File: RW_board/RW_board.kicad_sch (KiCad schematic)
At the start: 0 parts

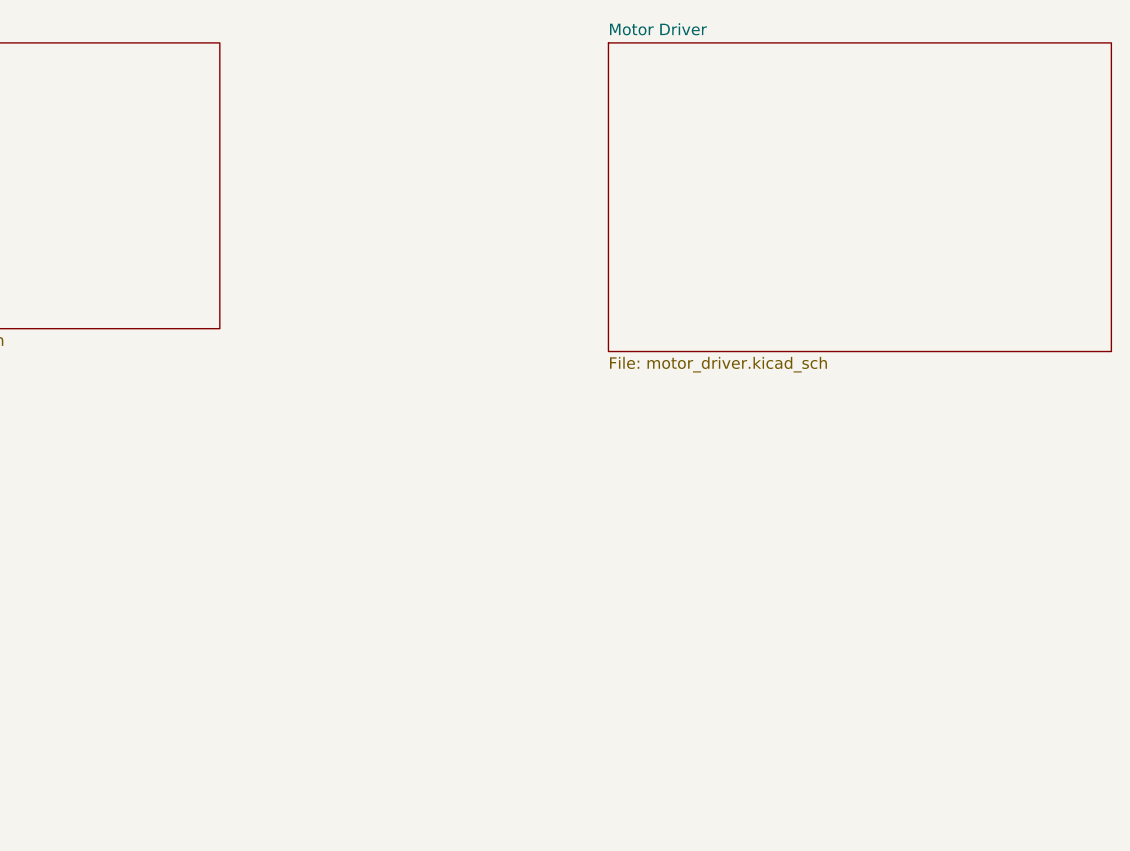
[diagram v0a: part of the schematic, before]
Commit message: Started working on motor driver schematic, added libraries, added motor cad
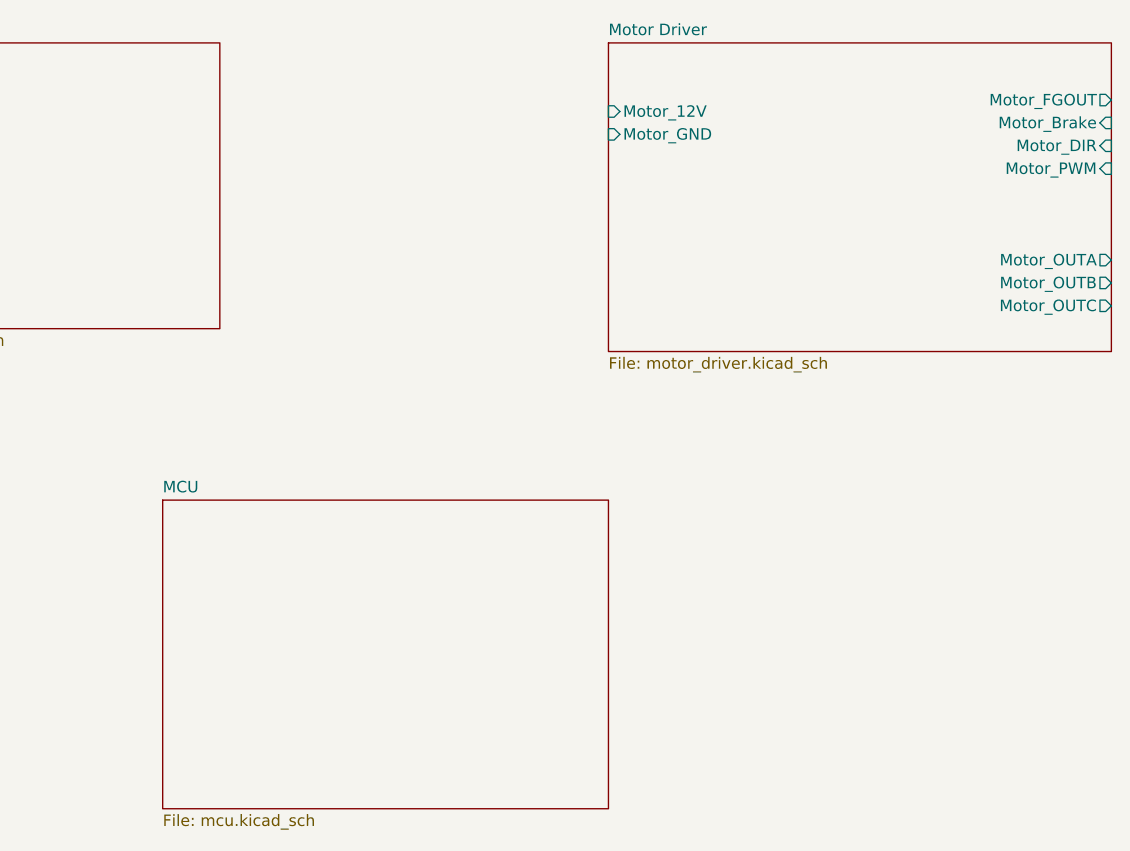
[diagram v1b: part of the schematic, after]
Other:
- added sheet MCU (mcu.kicad_sch)
- sheet Motor Driver ports: added Motor_12V, Motor_Brake, Motor_DIR, Motor_FGOUT, Motor_GND, Motor_OUTA, Motor_OUTB, Motor_OUTC, Motor_PWM; removed none
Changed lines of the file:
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@@
+			)
+		)
+		(pin "Motor_12V" input
+			(at 146.05 58.42 180)
+			(effects
+				(font
+					(size 1.27 1.27)
+				)
+				(justify left)
+			)
+		)
+		(pin "Motor_GND" input
+			(at 146.05 60.96 180)
+			(effects
+				(font
+					(size 1.27 1.27)
+				)
+				(justify left)
+			)
+		)
+		(pin "Motor_FGOUT" output
+			(at 201.93 57.15 0)
+			(effects
+				(font
+					(size 1.27 1.27)
+				)
+				(justify right)
+			)
+		)
+		(pin "Motor_Brake" input
+			(at 201.93 59.69 0)
+			(effects
+				(font
+					(size 1.27 1.27)
+				)
+				(justify right)
+			)
+		)
+		(pin "Motor_DIR" input
+			(at 201.93 62.23 0)
+			(effects
+				(font
+					(size 1.27 1.27)
+				)
+				(justify right)
+			)
+		)
+		(pin "Motor_PWM" input
+			(at 201.93 64.77 0)
+			(effects
+				(font
+					(size 1.27 1.27)
+				)
+				(justify right)
+			)
+		)
+		(pin "Motor_OUTB" output
+			(at 201.93 77.47 0)
+			(effects
+				(font
+					(size 1.27 1.27)
+				)
+				(justify right)
+			)
+		)
+		(pin "Motor_OUTC" output
+			(at 201.93 80.01 0)
+			(effects
+				(font
+					(size 1.27 1.27)
+				)
+				(justify right)
+			)
+		)
+		(pin "Motor_OUTA" output
+			(at 201.93 74.93 0)
+			(effects
+				(font
+					(size 1.27 1.27)
+				)
+				(justify right)
 			)
 		)
@@
 				)
 			)
+		)
+	)
+	(sheet
+		(at 96.52 101.6)
+		(size 49.53 34.29)
+		(fields_autoplaced yes)
+		(stroke
+			(width 0.1524)
+			(type solid)
+		)
+		(fill
+			(color 0 0 0 0.0000)
+		)
+		(property "Sheetname" "MCU"
+			(at 96.52 100.8884 0)
+			(effects
+				(font
+					(size 1.27 1.27)
+				)
+				(justify left bottom)
+			)
+		)
+		(property "Sheetfile" "mcu.kicad_sch"
+			(at 96.52 136.4746 0)
+			(effects
+				(font
+					(size 1.27 1.27)
+				)
+				(justify left top)
+			)
+		)
+		(instances
+			(project "RW_board"
+				(path "/ff273890-9ca6-499d-9c73-a93557b69e48"
+					(page "4")
+				)
+			)

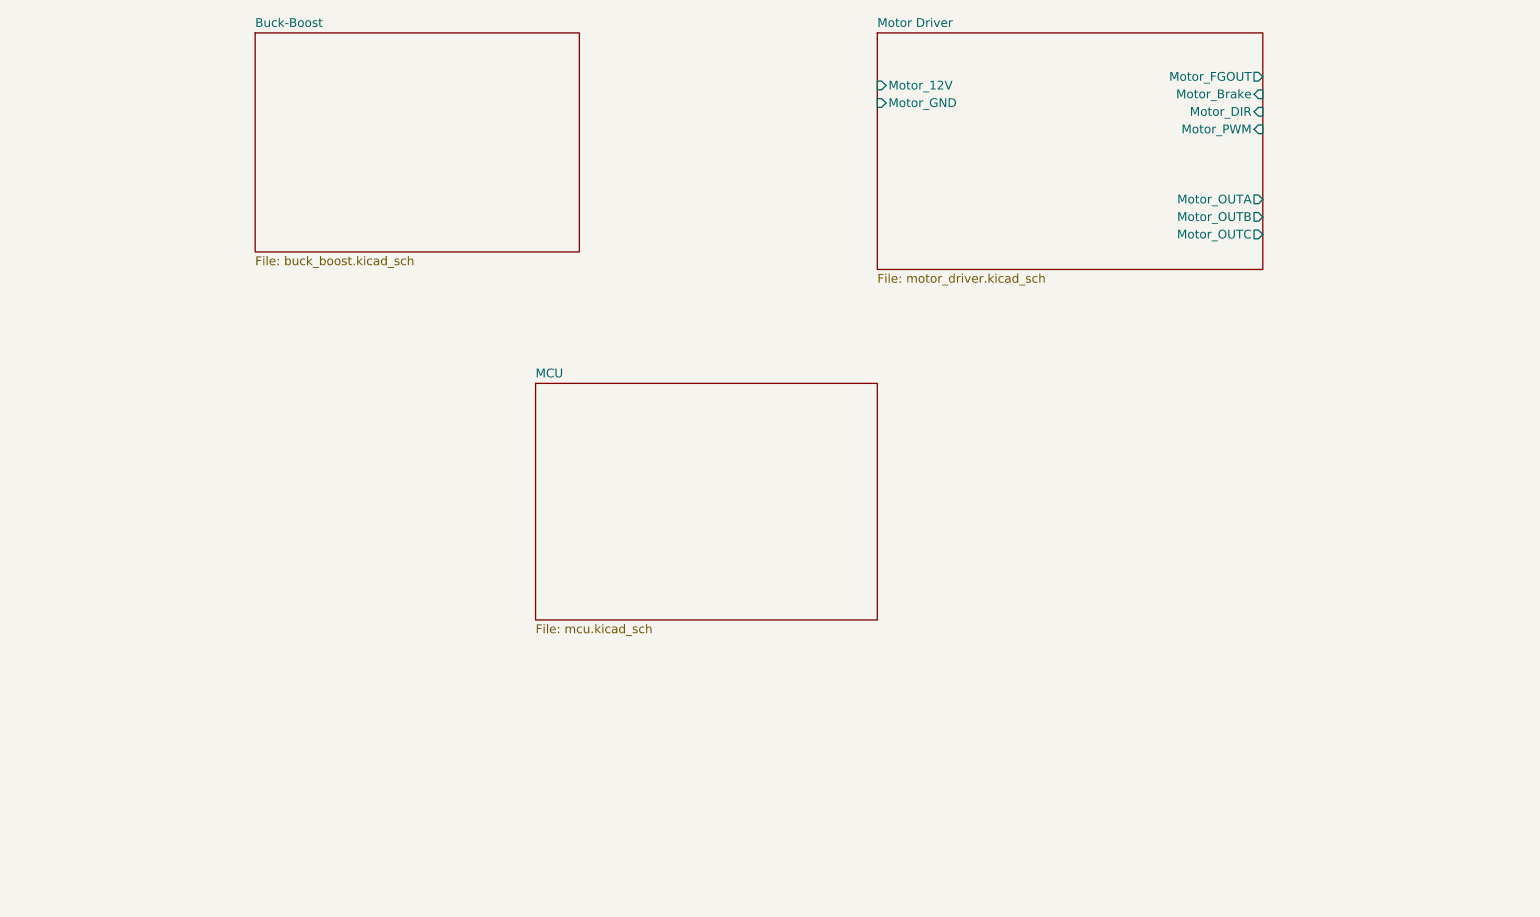
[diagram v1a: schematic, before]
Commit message: Added motor symbol/footprint, worked more on schematic
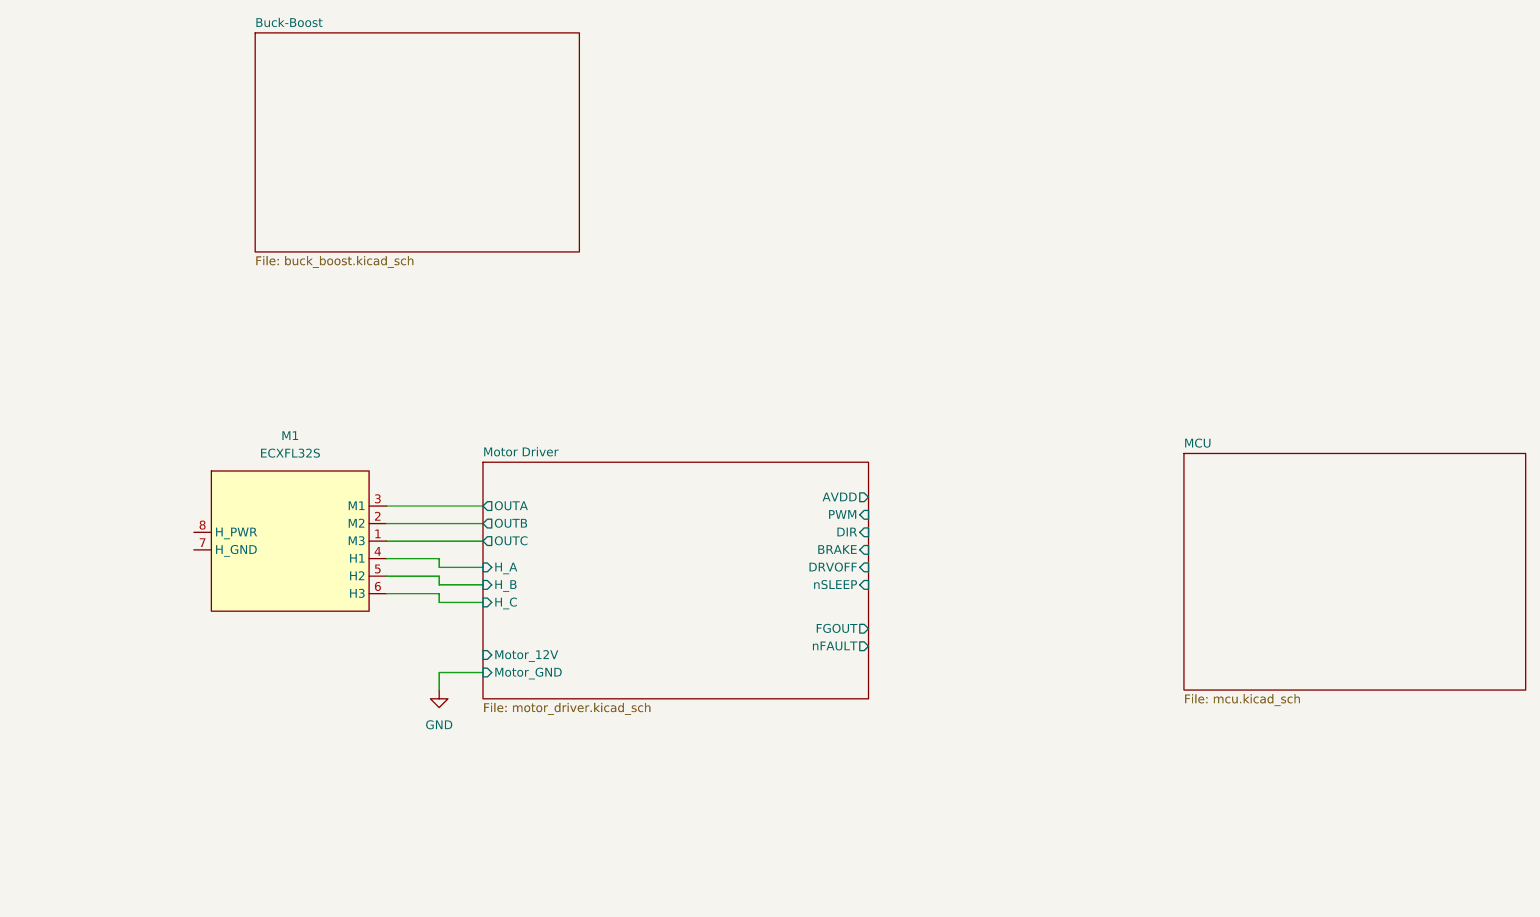
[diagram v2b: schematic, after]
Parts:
- added M1: ECXFL32S, ECXFL32S:ECXFL32S, symbol ECXFL32S:ECXFL32S
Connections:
- new net Motor Driver/H_A: M1.4 (H1)
- new net Motor Driver/H_B: M1.5 (H2)
- new net Motor Driver/H_C: M1.6 (H3)
- new net Motor Driver/OUTA: M1.3 (M1)
- new net Motor Driver/OUTB: M1.2 (M2)
- new net Motor Driver/OUTC: M1.1 (M3)
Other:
- sheet Motor Driver ports: added AVDD, BRAKE, DIR, DRVOFF, FGOUT, H_A, H_B, H_C, OUTA, OUTB, OUTC, PWM, nFAULT, nSLEEP; removed Motor_Brake, Motor_DIR, Motor_FGOUT, Motor_OUTA, Motor_OUTB, Motor_OUTC, Motor_PWM

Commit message: Completed MCU schematic, connected with driver schematic
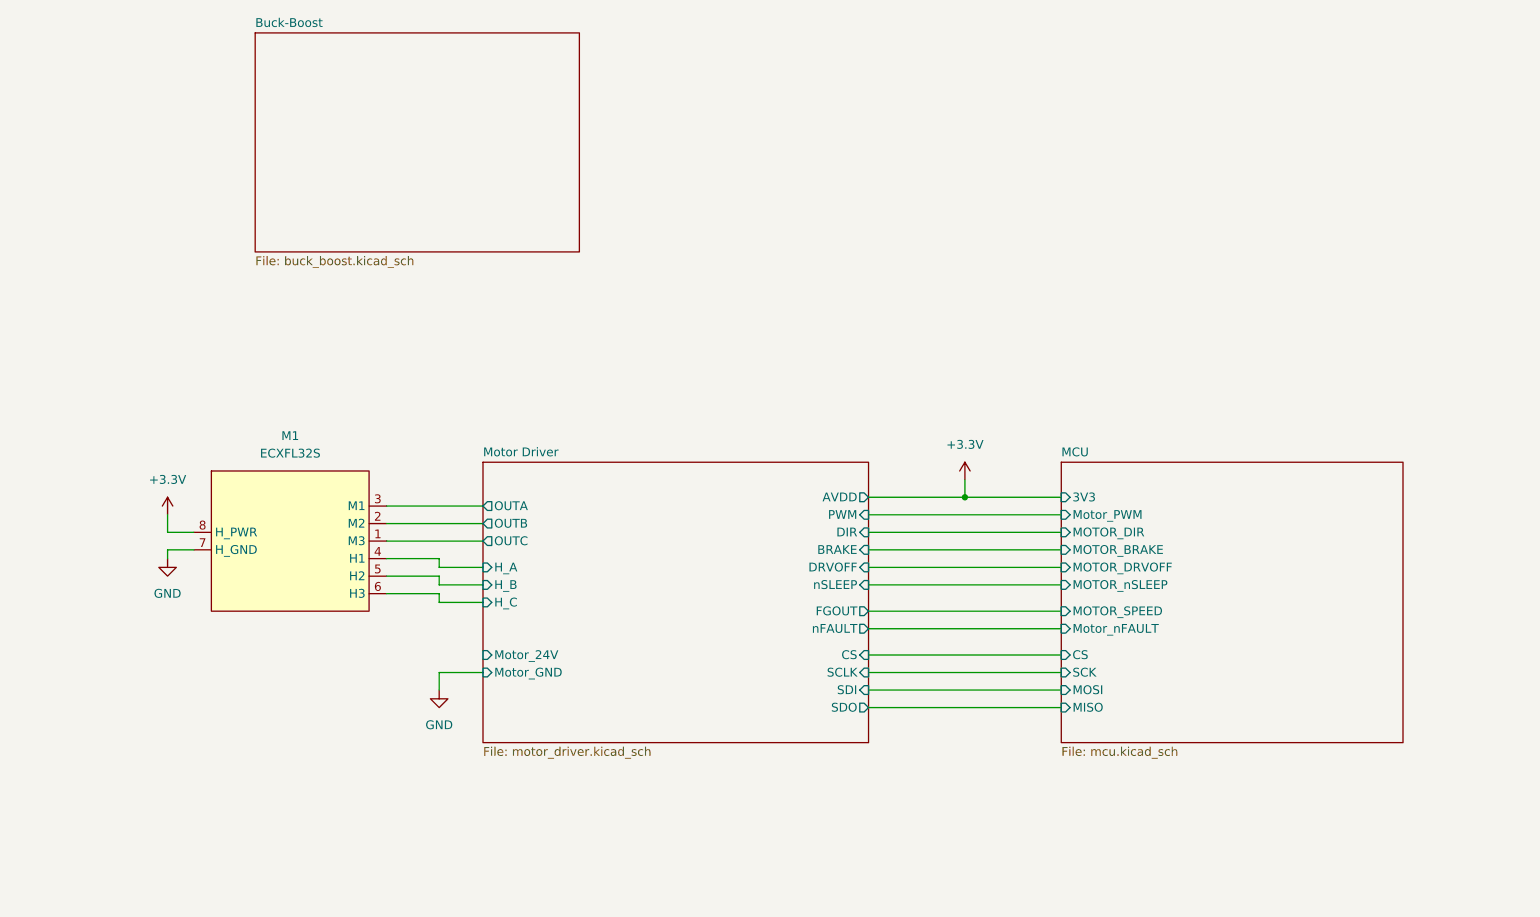
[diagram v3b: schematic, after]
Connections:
- net GND: now also M1.7 (H_GND)
- net +3.3V: now reaches M1.8 (H_PWR)
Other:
- sheet MCU ports: added 3V3, CS, MISO, MOSI, MOTOR_BRAKE, MOTOR_DIR, MOTOR_DRVOFF, MOTOR_SPEED, MOTOR_nSLEEP, Motor_PWM, Motor_nFAULT, SCK; removed none
- sheet Motor Driver ports: added CS, Motor_24V, SCLK, SDI, SDO; removed Motor_12V

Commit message: Switched motor, added connectors, finished up design
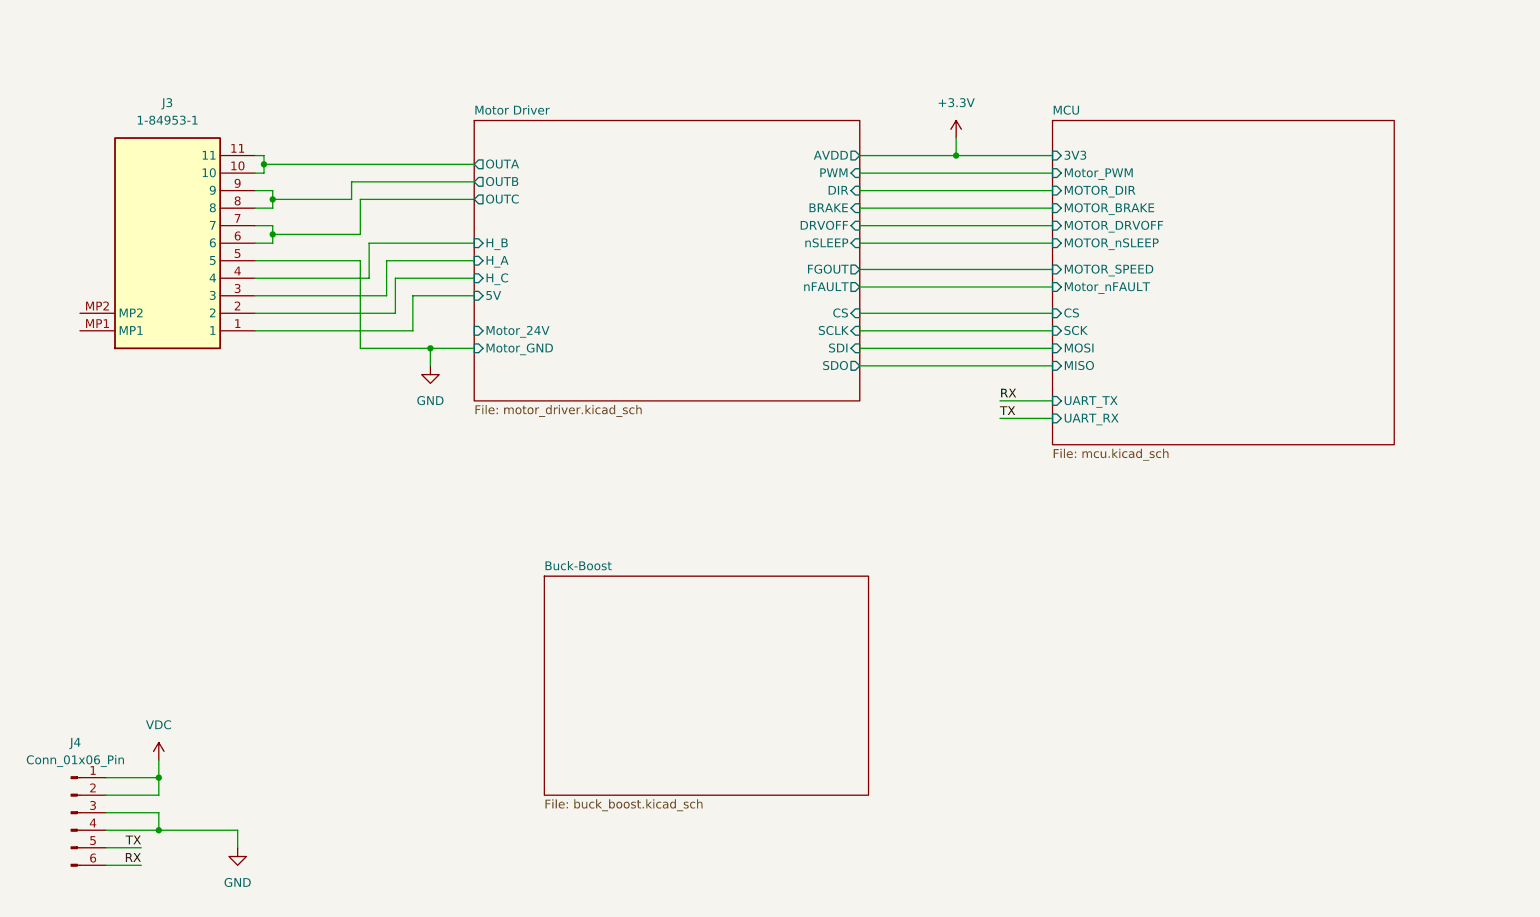
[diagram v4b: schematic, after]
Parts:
- removed M1: ECXFL32S, ECXFL32S:ECXFL32S, symbol ECXFL32S:ECXFL32S
- added J3: 1-84953-1, 1849531, symbol RW_Imports:1-84953-1
- added J4: Conn_01x06_Pin, symbol Connector:Conn_01x06_Pin
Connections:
- net GND: now also J3.5, J4.3 (Pin_3), J4.4 (Pin_4)
- net Motor Driver/H_A: now also J3.3
- net Motor Driver/H_B: now also J3.4
- net Motor Driver/H_C: now also J3.2
- net Motor Driver/OUTA: now also J3.10, J3.11
- net Motor Driver/OUTB: now also J3.8, J3.9
- net Motor Driver/OUTC: now also J3.6, J3.7
- new net Motor Driver/5V: J3.1
- new net RX: J4.6 (Pin_6)
- new net TX: J4.5 (Pin_5)
- new net VDC: J4.1 (Pin_1), J4.2 (Pin_2)
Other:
- sheet MCU ports: added UART_RX, UART_TX; removed none
- sheet Motor Driver ports: added 5V; removed none

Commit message: Picoblade footprint
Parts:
- J4: footprint (none) -> Connector_Molex:Molex_PicoBlade_53048-0610_1x06_P1.25mm_Horizontal
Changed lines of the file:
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@@
 			)
 		)
-		(property "Footprint" ""
+		(property "Footprint" "Connector_Molex:Molex_PicoBlade_53048-0610_1x06_P1.25mm_Horizontal"
 			(at 29.21 163.83 0)
 			(effects

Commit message: Fixed reset switch
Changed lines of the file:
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@@
-	)
-	(junction
-		(at 157.48 68.58)
-		(diameter 0)
-		(color 0 0 0 0)
 	)
 	(junction
@@
 	(wire
 		(pts
-			(xy 157.48 68.58) (xy 171.45 68.58)
-		)
-		(stroke
-			(width 0)
-			(type default)
-		)
-	)
-	(wire
-		(pts
 			(xy 163.83 104.14) (xy 171.45 104.14)
 		)
@@
 	(wire
 		(pts
-			(xy 157.48 66.04) (xy 157.48 68.58)
-		)
-		(stroke
-			(width 0)
-			(type default)
-		)
-	)
-	(wire
-		(pts
 			(xy 55.88 81.28) (xy 58.42 81.28)
 		)
@@
 	(wire
 		(pts
-			(xy 143.51 68.58) (xy 157.48 68.58)
+			(xy 143.51 68.58) (xy 171.45 68.58)
 		)
 		(stroke
@@
 					(unit 1)
 				)
-			)
-		)
-	)
-	(symbol
-		(lib_id "power:+3.3V")
-		(at 157.48 66.04 0)
-		(unit 1)
-		(exclude_from_sim no)
-		(in_bom yes)
-		(on_board yes)
-		(dnp no)
-		(fields_autoplaced yes)
-		(property "Reference" "#PWR019"
-			(at 157.48 69.85 0)
-			(effects
-				(font
-					(size 1.27 1.27)
-				)
-				(hide yes)
-			)
-		)
-		(property "Value" "+3.3V"
-			(at 157.48 60.96 0)
-			(effects
-				(font
-					(size 1.27 1.27)
-				)
-			)
-		)
-		(property "Footprint" ""
-			(at 157.48 66.04 0)
-			(effects
-				(font
-					(size 1.27 1.27)
-				)
-				(hide yes)
-			)
-		)
-		(property "Datasheet" ""
-			(at 157.48 66.04 0)
-			(effects
-				(font
-					(size 1.27 1.27)
-				)
-				(hide yes)
-			)
-		)
-		(property "Description" "Power symbol creates a global label with name \"+3.3V\""
-			(at 157.48 66.04 0)
-			(effects
-				(font
-					(size 1.27 1.27)
-				)
-				(hide yes)
-			)
-		)
-		(pin "1"
-		)
-		(instances
-			(project ""
-				(path "/ff273890-9ca6-499d-9c73-a93557b69e48"
-					(reference "#PWR019")
-					(unit 1)
-				)
